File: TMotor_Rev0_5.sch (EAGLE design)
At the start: 105 parts, among them U1 INA125U, U10 DEV-16771, U2 INA125U, U3 INA125U, U4 INA125U, U5 SN65HVD230MDREP, U6 2SJ305TE85LF, U7 2SJ305TE85LF, U8 2SJ305TE85LF, U9 2SJ305TE85LF

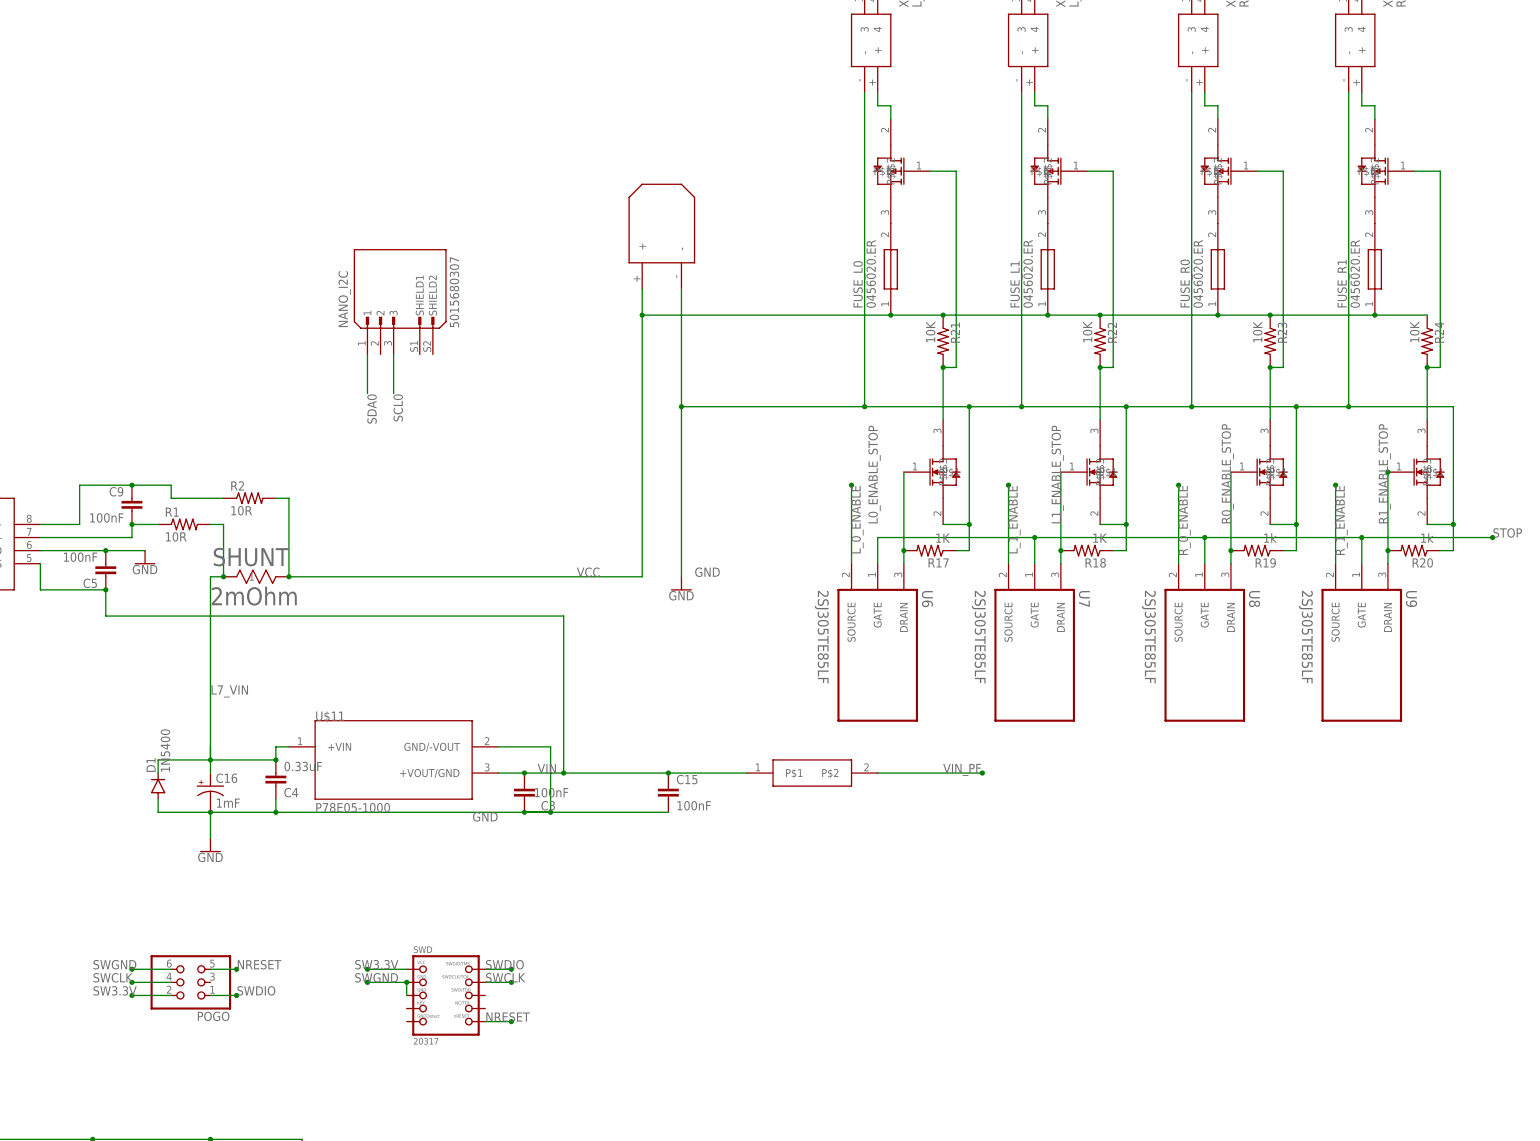
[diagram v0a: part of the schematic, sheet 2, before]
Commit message: Removed Power FETS, power FET supporting hardware, and SWD IO for nano
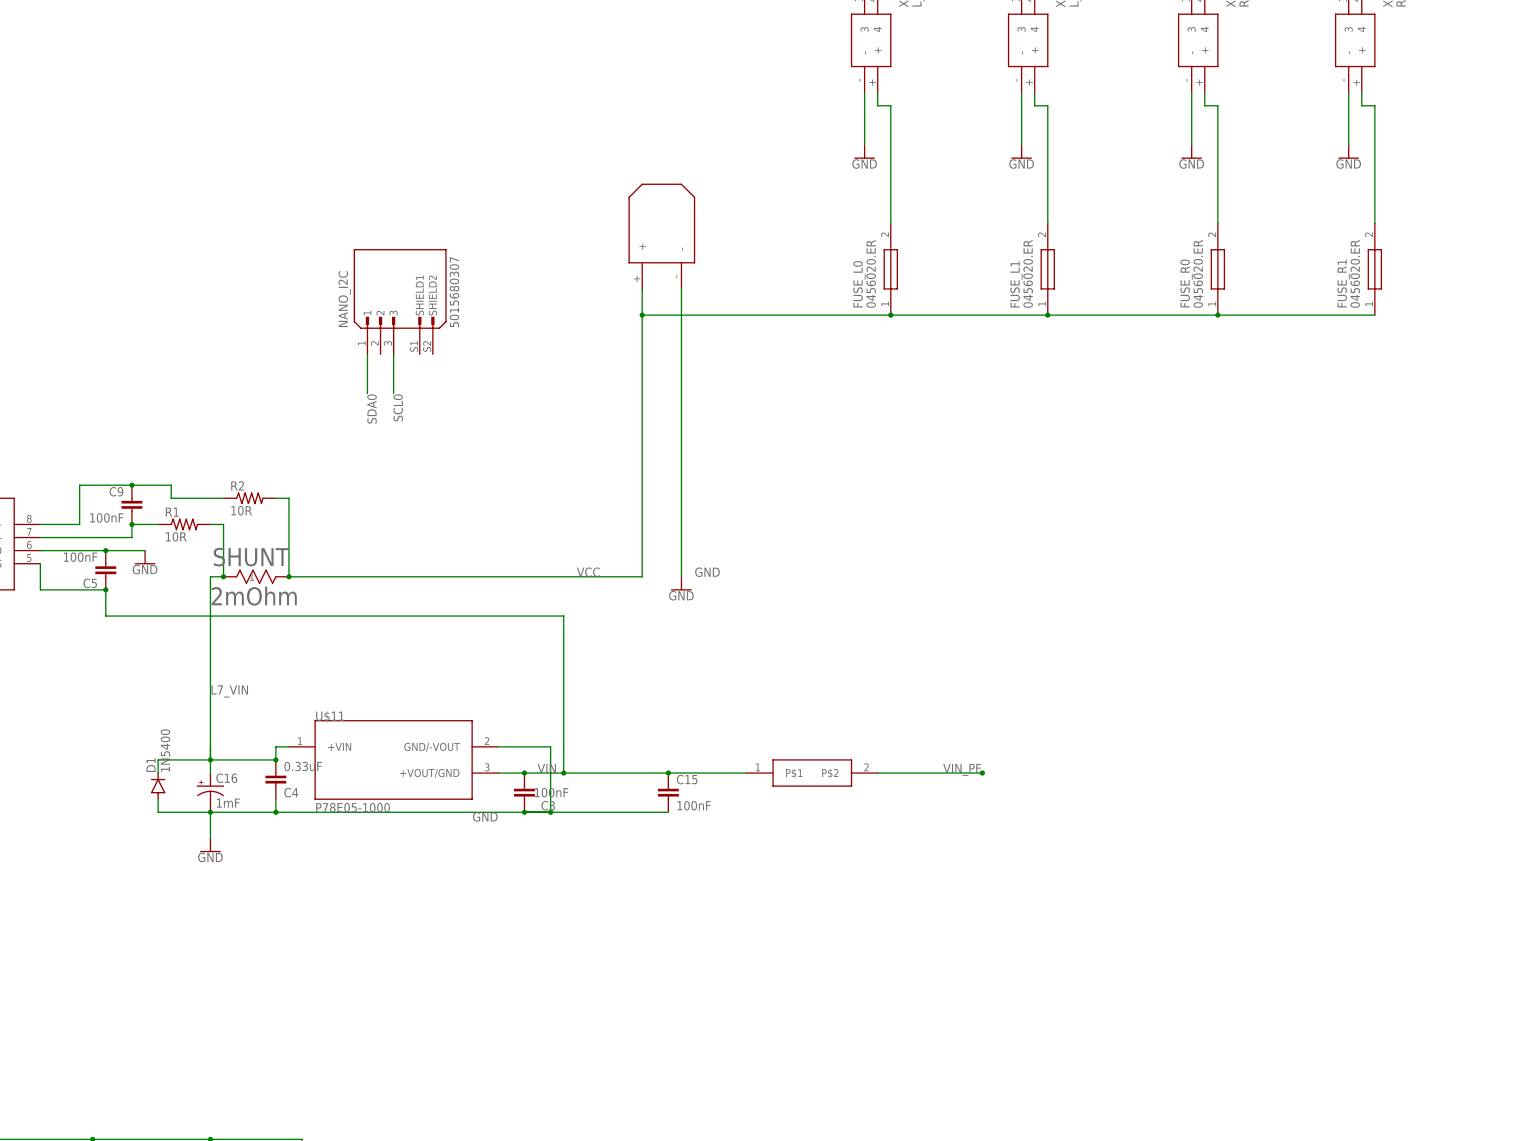
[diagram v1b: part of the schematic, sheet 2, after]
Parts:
- removed POGO: (no value), pinhead:PINHD-2X3
- removed R17, R18: 1K, rcl:R-US_0207/10
- removed R19, R20: 1k, rcl:R-US_0207/10
- removed R21, R22, R23, R24: 10K, rcl:R-US_0207/10
- removed SWD: 20317, microbuilder:JTAG-CORTEXBOXPOSTS
- removed U$1, U$2, U$3, U$4: SSM3K329R, SnapEDA-Library:SSM3K329R
- removed U$10, U$5, U$7, U$8: FQP12P20, SnapEDA-Library:FQP12P20
- removed U6, U7, U8, U9: 2SJ305TE85LF, 2SJ305TE85LF:2SJ305TE85LF
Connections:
- removed net L0_ENABLE_STOP: R17.2, U$1.P$1, U6.DRAIN
- removed net L1_ENABLE_STOP: R18.2, U$2.P$1, U7.DRAIN
- removed net L_0_ENABLE: U10.RX7, U6.SOURCE
- removed net L_1_ENABLE: U10.TX7, U7.SOURCE
- removed net MISO: U10.MOSI, USB.D12
- removed net MOSI: U10.MISO, USB.D11
- removed net N$43: R21.2, U$1.P$3, U$5.P$1
- removed net N$46: FUSE_R1.2, U$10.P$3
- removed net N$47: R23.2, U$3.P$3, U$8.P$1
- removed net N$48: R22.2, U$2.P$3, U$7.P$1
- removed net N$49: R24.2, U$10.P$1, U$4.P$3
- removed net N$50: FUSE_R0.2, U$8.P$3
- removed net N$51: FUSE_L1.2, U$7.P$3
- removed net N$52: FUSE_L0.2, U$5.P$3
- removed net NANO_CS: U10.CS1, USB.D10
- removed net NRESET: POGO.5, SWD.NRESET
- removed net R0_ENABLE_STOP: R19.2, U$3.P$1, U8.DRAIN
- removed net R1_ENABLE_STOP: R20.2, U$4.P$1, U9.DRAIN
- removed net R_0_ENABLE: U10.TX2, U8.SOURCE
- removed net R_1_ENABLE: U10.RX2, U9.SOURCE
- removed net SW3.3V: POGO.2, SWD.VCC
- removed net SWCLK: POGO.4, SWD.SWDCLK
- removed net SWDIO: POGO.1, SWD.SWDIO
- removed net SWGND: POGO.6, SWD.GND@1, SWD.GND@2
- net GND: no longer R17.1, R18.1, R19.1, R20.1, U$1.P$2, U$2.P$2, U$3.P$2, U$4.P$2
- net N$53: now also FUSE_L0.2; no longer U$5.P$2
- net N$54: now also FUSE_L1.2; no longer U$7.P$2
- net N$55: now also FUSE_R0.2; no longer U$8.P$2
- net N$56: now also FUSE_R1.2; no longer U$10.P$2
- net SCK: no longer USB.D13
- net STOP: no longer U10.OUT1C, U6.GATE, U7.GATE, U8.GATE, U9.GATE
- net VCC: no longer R21.1, R22.1, R23.1, R24.1
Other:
- note removed: "MISO and MOSI intentionally flipped"

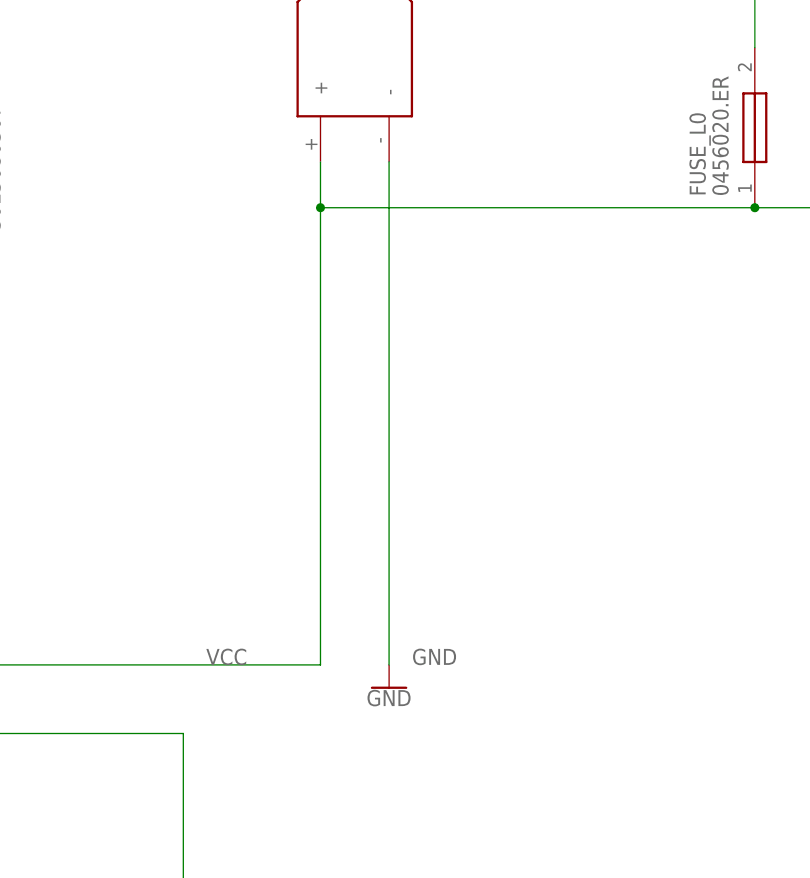
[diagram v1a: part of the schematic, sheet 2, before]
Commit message: Added serial connection between nano and teensy
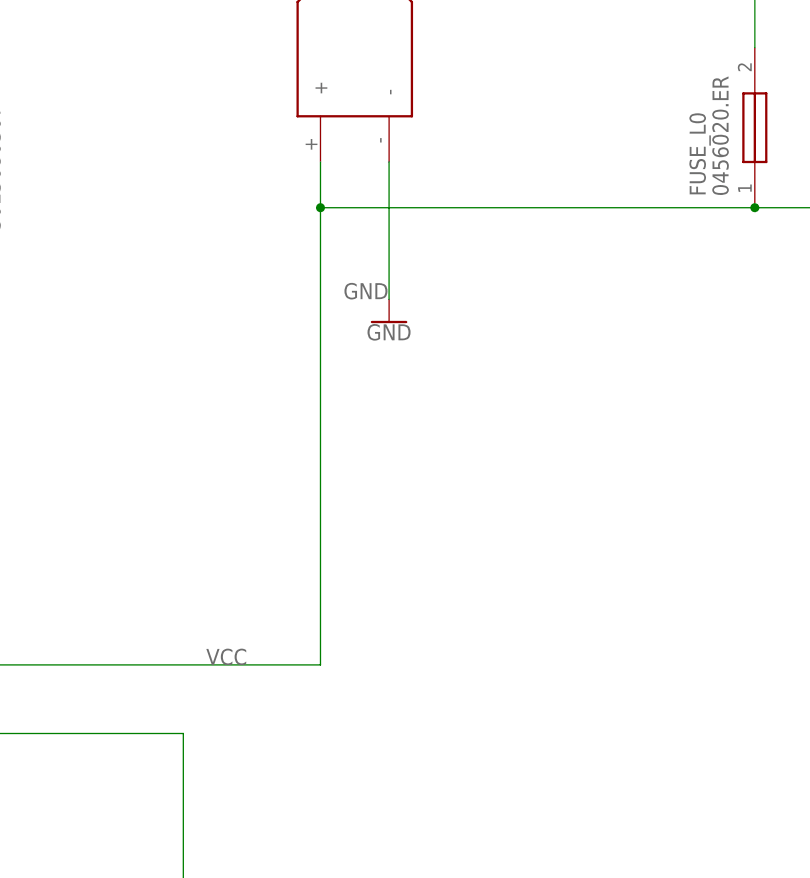
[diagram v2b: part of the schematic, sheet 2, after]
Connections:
- new net NANO_RX: U10.TX8, USB.RX0
- new net NANO_TX: U10.RX8, USB.TX1
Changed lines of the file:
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@@
+</segment>
+</net>
+<net name="NANO_RX" class="0">
+<segment>
+<pinref part="USB" gate="G$1" pin="RX0"/>
+<wire x1="91.44" y1="7.62" x2="99.06" y2="7.62" width="0.1524" layer="91"/>
+<label x="93.98" y="7.62" size="1.778" layer="95"/>
+</segment>
+<segment>
+<pinref part="U10" gate="G$1" pin="TX8"/>
+<wire x1="147.32" y1="50.8" x2="137.16" y2="50.8" width="0.1524" layer="91"/>
+<label x="134.62" y="48.26" size="1.778" layer="95"/>
+</segment>
+</net>
+<net name="NANO_TX" class="0">
+<segment>
+<pinref part="USB" gate="G$1" pin="TX1"/>
+<wire x1="91.44" y1="5.08" x2="99.06" y2="5.08" width="0.1524" layer="91"/>
+<label x="93.98" y="2.54" size="1.778" layer="95"/>
+</segment>
+<segment>
+<pinref part="U10" gate="G$1" pin="RX8"/>
+<wire x1="147.32" y1="53.34" x2="137.16" y2="53.34" width="0.1524" layer="91"/>
+<label x="134.62" y="53.34" size="1.778" layer="95"/>
 </segment>
 </net>
@@
 <attribute name="VALUE" x="-156.21" y="215.138" size="1.778" layer="96"/>
 </instance>
-<instance part="GND5" gate="1" x="-68.58" y="200.66" smashed="yes" rot="MR0">
-<attribute name="VALUE" x="-68.58" y="200.406" size="1.778" layer="96" rot="MR0" align="top-center"/>
+<instance part="GND5" gate="1" x="-68.58" y="241.3" smashed="yes" rot="MR0">
+<attribute name="VALUE" x="-68.58" y="241.046" size="1.778" layer="96" rot="MR0" align="top-center"/>
 </instance>
 <instance part="U$9" gate="G$1" x="-71.12" y="264.16" smashed="yes" rot="R90"/>
@@
 <pinref part="U$9" gate="G$1" pin="-"/>
 <pinref part="GND5" gate="1" pin="GND"/>
-<wire x1="-68.58" y1="203.2" x2="-68.58" y2="259.08" width="0.1524" layer="91"/>
-<label x="-66.04" y="203.2" size="1.778" layer="95"/>
-</segment>
-<segment>
+<wire x1="-68.58" y1="243.84" x2="-68.58" y2="259.08" width="0.1524" layer="91"/>
+<label x="-73.66" y="243.84" size="1.778" layer="95"/>
+</segment>
+<segment>

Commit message: Added Upright Power connectors
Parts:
- removed FUSE_R0, FUSE_R1: 0456020.ER, SamacSys_Parts:0456020.ER
- removed L_0, L_1, R_0, R_1: XT30PW-F, XT30PW-M:XT30PW-F
- removed U$9: XT30, Ben_Library:XT30
- added FUSE_L2, FUSE_L3: 0456020.ER, SamacSys_Parts:0456020.ER
- added XT30UPB-F, XT30UPB-F1, XT30UPB-F2, XT30UPB-F3, XT30UPB-F4: L_0, XT30UPB-F:XT30UPB-F
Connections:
- removed net N$54: FUSE_L1.2, L_1.+
- removed net N$55: FUSE_R0.2, R_0.+
- removed net N$56: FUSE_R1.2, R_1.+
- new net N$43: FUSE_L1.2
- new net N$46: FUSE_L2.2
- new net N$47: FUSE_L3.2
- new net VCC1: FUSE_L1.1
- new net VCC2: FUSE_L2.1
- new net VCC3: FUSE_L3.1
- net GND: no longer L_0.-, L_1.-, R_0.-, R_1.-, U$9.-
- net N$53: no longer L_0.+
- net VCC: no longer FUSE_L1.1, FUSE_R0.1, FUSE_R1.1, U$9.+
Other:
- moved on the sheet: FUSE_L0, FUSE_L1
